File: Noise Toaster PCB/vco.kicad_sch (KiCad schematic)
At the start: 22 parts, among them Q3 2N3904, Q4 2N3904, U1 LM324

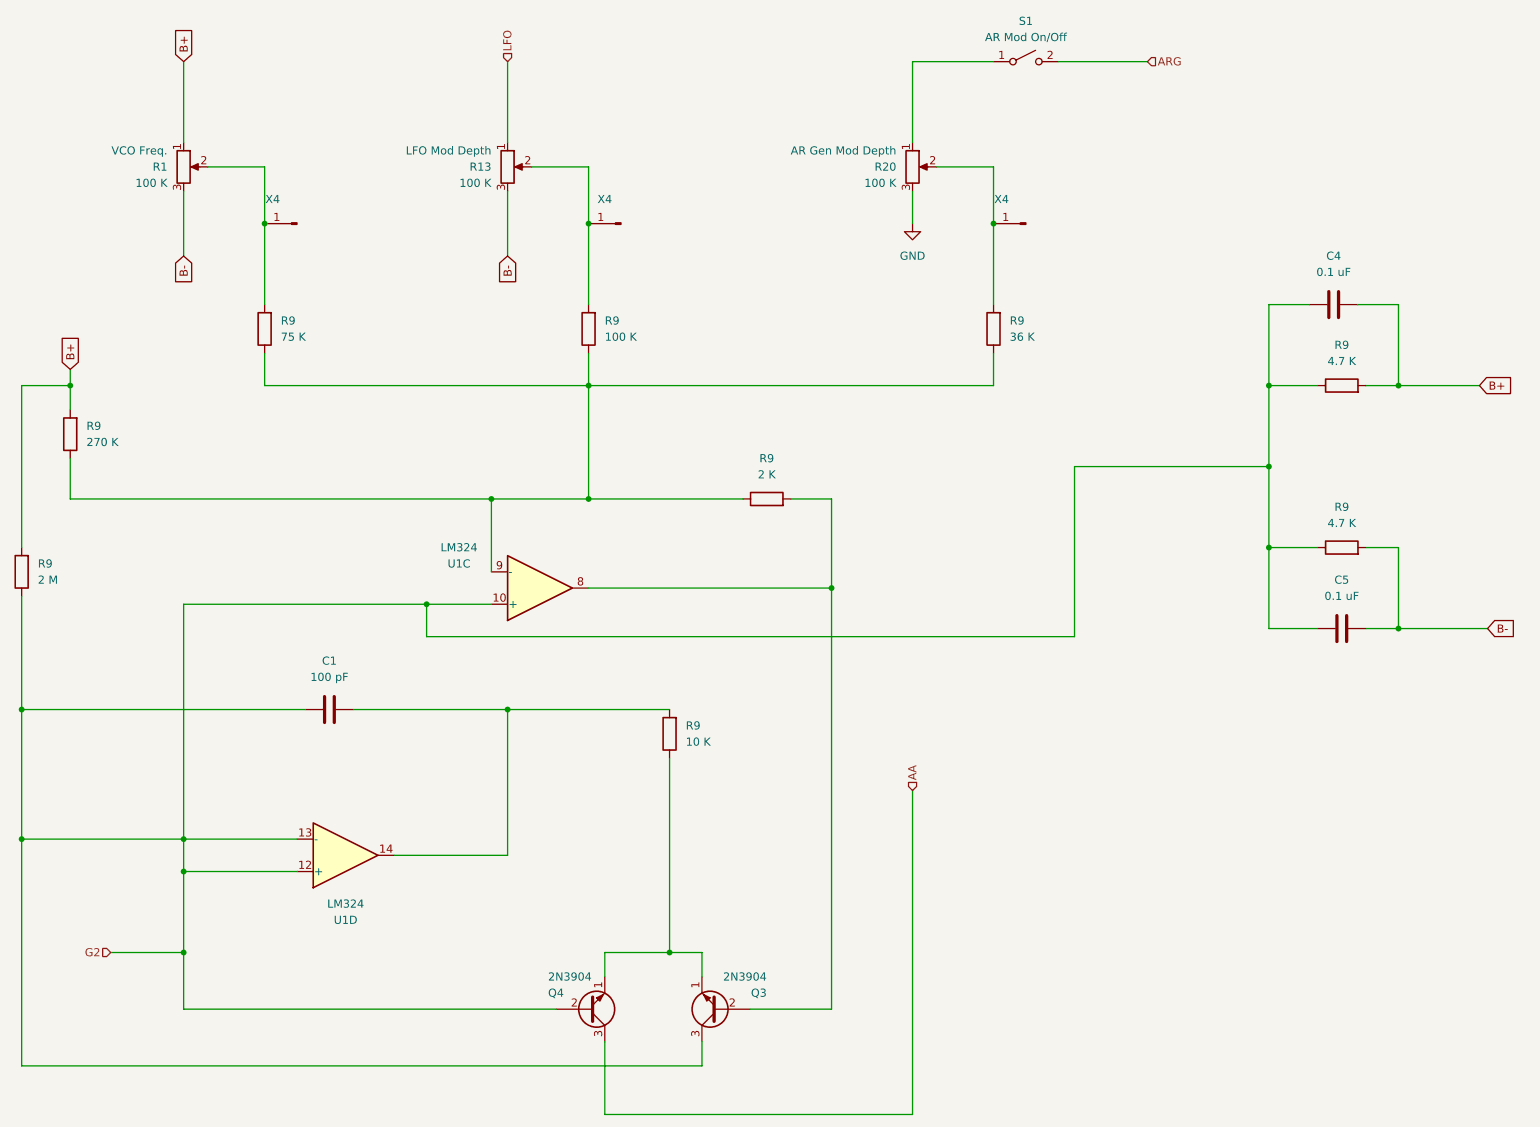
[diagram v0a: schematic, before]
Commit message: updated schematics
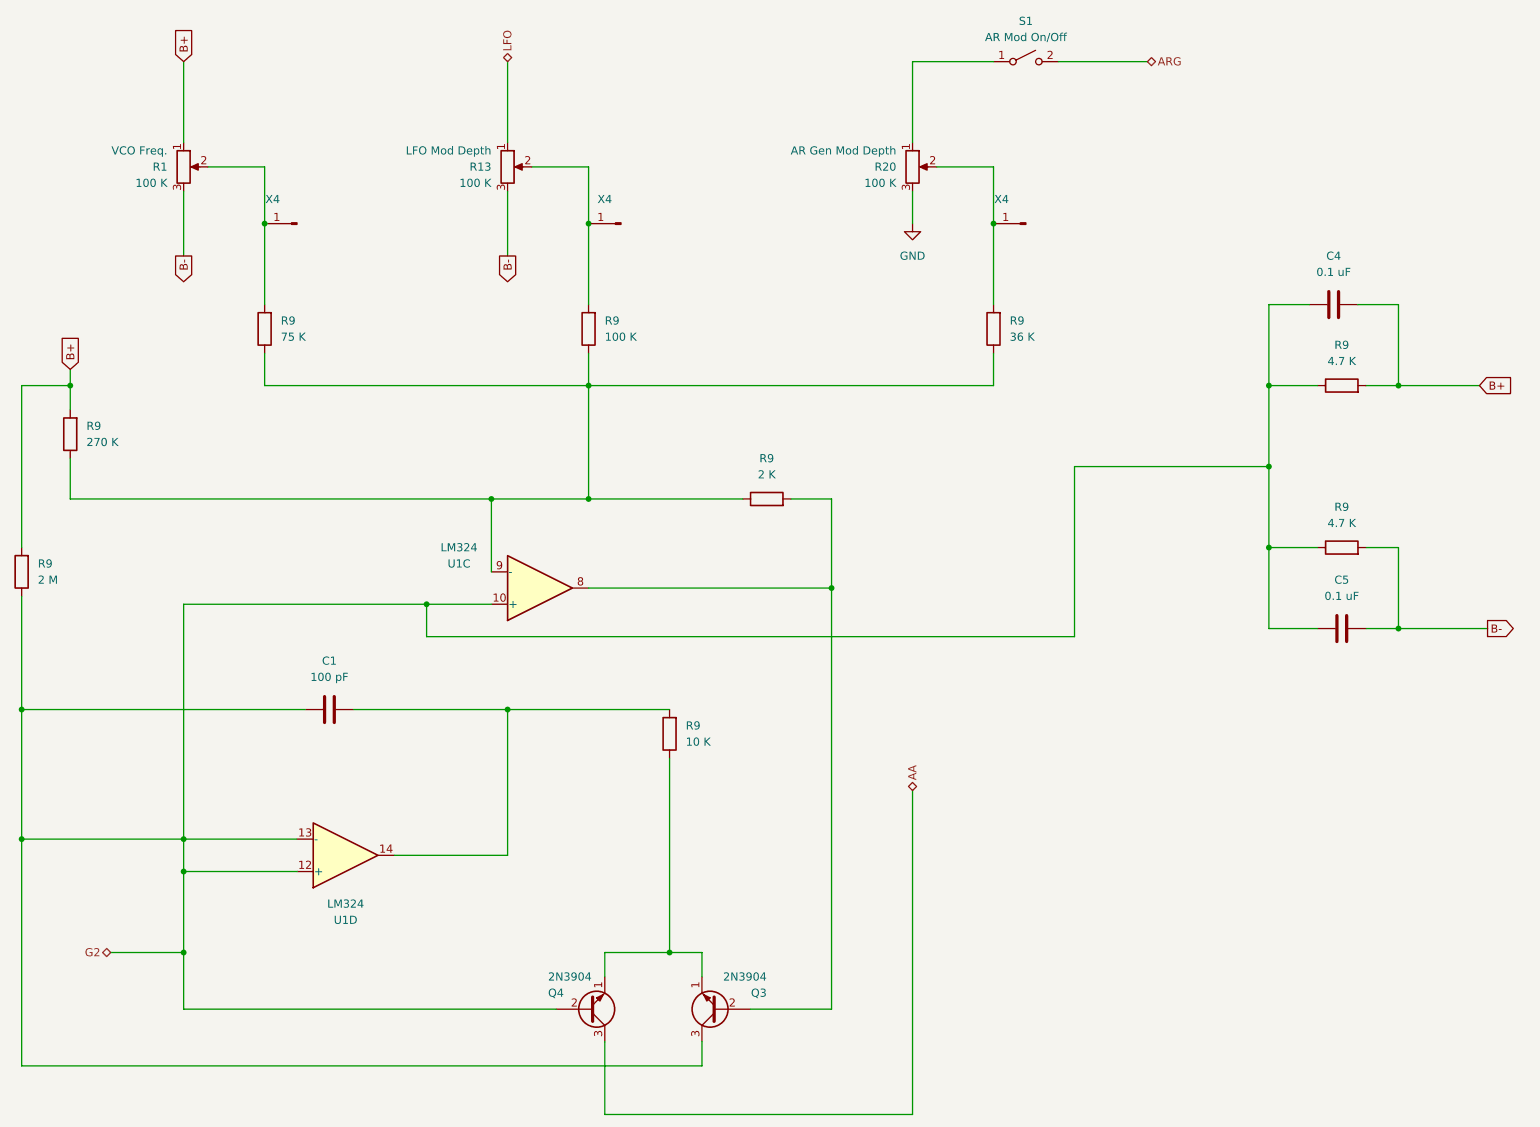
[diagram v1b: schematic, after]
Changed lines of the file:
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@@
     (stroke (width 0) (type default))
   )
-  (global_label "B-" (shape input) (at 255.27 114.3 0) (fields_autoplaced)
+  (global_label "B-" (shape output) (at 255.27 114.3 0) (fields_autoplaced)
     (effects (font (size 1.27 1.27)) (justify left))
     (property "Intersheetrefs" "${INTERSHEET_REFS}" (at 261.0976 114.3 0)
@@
     )
   )
-  (global_label "B-" (shape input) (at 50.8 55.88 270) (fields_autoplaced)
+  (global_label "B-" (shape output) (at 50.8 55.88 270) (fields_autoplaced)
     (effects (font (size 1.27 1.27)) (justify right))
     (property "Intersheetrefs" "${INTERSHEET_REFS}" (at 50.8 61.7076 90)
@@
     )
   )
-  (global_label "B-" (shape input) (at 101.6 55.88 270) (fields_autoplaced)
+  (global_label "B-" (shape output) (at 101.6 55.88 270) (fields_autoplaced)
     (effects (font (size 1.27 1.27)) (justify right))
     (property "Intersheetrefs" "${INTERSHEET_REFS}" (at 101.6 61.7076 90)
@@
     )
   )
-  (hierarchical_label "ARG" (shape input) (at 201.93 25.4 0) (fields_autoplaced)
-    (effects (font (size 1.27 1.27)) (justify left))
-  )
-  (hierarchical_label "G2" (shape input) (at 39.37 165.1 180) (fields_autoplaced)
+  (hierarchical_label "ARG" (shape bidirectional) (at 201.93 25.4 0) (fields_autoplaced)
+    (effects (font (size 1.27 1.27)) (justify left))
+  )
+  (hierarchical_label "G2" (shape bidirectional) (at 39.37 165.1 180) (fields_autoplaced)
     (effects (font (size 1.27 1.27)) (justify right))
   )
-  (hierarchical_label "LFO" (shape input) (at 101.6 25.4 90) (fields_autoplaced)
-    (effects (font (size 1.27 1.27)) (justify left))
-  )
-  (hierarchical_label "AA" (shape input) (at 165.1 139.7 90) (fields_autoplaced)
+  (hierarchical_label "LFO" (shape bidirectional) (at 101.6 25.4 90) (fields_autoplaced)
+    (effects (font (size 1.27 1.27)) (justify left))
+  )
+  (hierarchical_label "AA" (shape bidirectional) (at 165.1 139.7 90) (fields_autoplaced)
     (effects (font (size 1.27 1.27)) (justify left))
   )
@@
     (instances
       (project "Noise Toaster PCB"
-        (path "/7be3f398-d902-4566-9ee4-0bff072cd47e/9c6b1f0b-dddb-43c5-83ba-4fcd1cf28662"
-          (reference "#PWR01") (unit 1)
-        )
         (path "/7be3f398-d902-4566-9ee4-0bff072cd47e/d0369b76-3398-4137-86ba-22490a5aca99"
           (reference "#PWR03") (unit 1)

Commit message: refactored the schematic
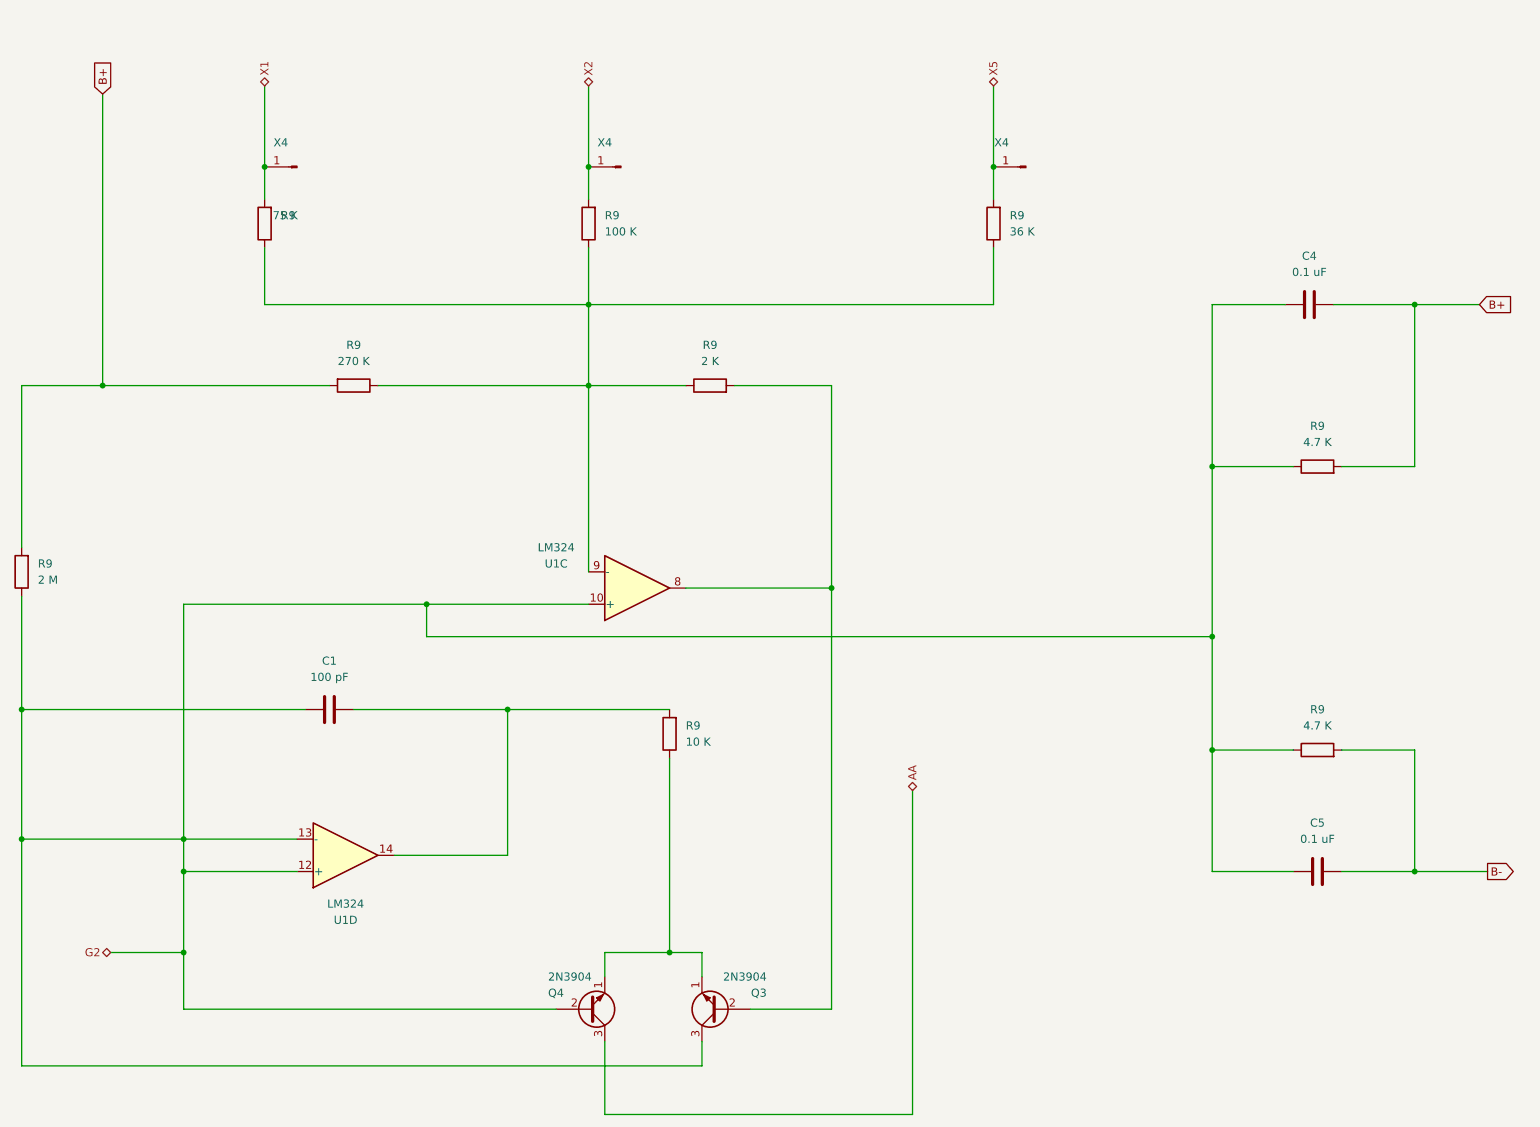
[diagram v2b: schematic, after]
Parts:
- removed R1, R13, R20: 100 K, symbol Device:R_Potentiometer
- removed S1: AR Mod On/Off, symbol Switch:SW_SPST
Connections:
- net X1: now reaches R9.2, X4.1 (Pin_1)
- net X5: now reaches R9.2, X4.1 (Pin_1)
- net X2: now reaches R9.2, X4.1 (Pin_1)
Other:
- moved on the sheet: C4, C5, R9, U1C, X4

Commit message: wireing and components have been checked
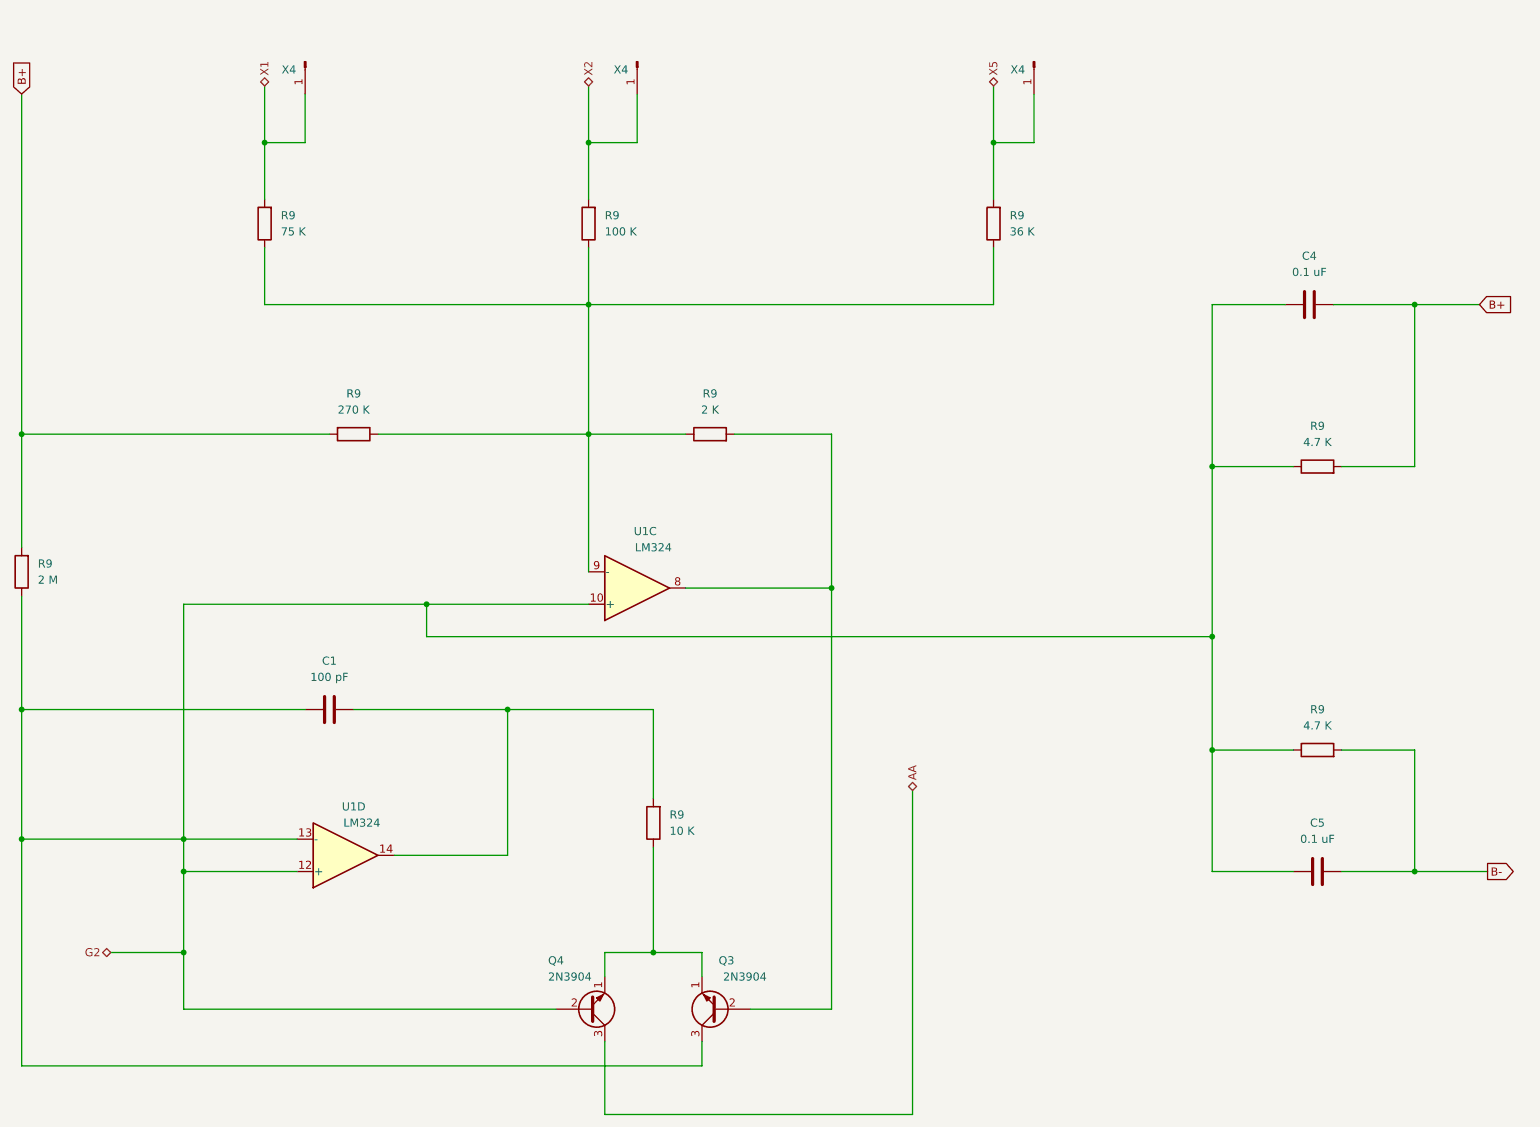
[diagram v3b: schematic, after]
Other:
- moved on the sheet: R9, X4

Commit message: applied footprints
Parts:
- C1, C4, C5: footprint (none) -> Capacitor_THT:C_Disc_D5.1mm_W3.2mm_P5.00mm
- R9: footprint (none) -> Resistor_THT:R_Axial_DIN0207_L6.3mm_D2.5mm_P10.16mm_Horizontal
- U1: footprint (none) -> Package_DIP:DIP-14_W7.62mm_Socket
- X4: footprint (none) -> Connector_PinHeader_1.00mm:PinHeader_1x01_P1.00mm_Vertical
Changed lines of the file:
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@@
       (effects (font (size 1.27 1.27)))
     )
-    (property "Footprint" "" (at 77.47 82.042 90)
+    (property "Footprint" "Resistor_THT:R_Axial_DIN0207_L6.3mm_D2.5mm_P10.16mm_Horizontal" (at 77.47 82.042 90)
       (effects (font (size 1.27 1.27)) hide)
     )
@@
       (effects (font (size 1.27 1.27)))
     )
-    (property "Footprint" "" (at 231.14 62.5348 0)
+    (property "Footprint" "Capacitor_THT:C_Disc_D5.1mm_W3.2mm_P5.00mm" (at 231.14 62.5348 0)
       (effects (font (size 1.27 1.27)) hide)
     )
@@
       (effects (font (size 1.27 1.27)))
     )
-    (property "Footprint" "" (at 228.6 90.678 90)
+    (property "Footprint" "Resistor_THT:R_Axial_DIN0207_L6.3mm_D2.5mm_P10.16mm_Horizontal" (at 228.6 90.678 90)
       (effects (font (size 1.27 1.27)) hide)
     )
@@
       (effects (font (size 1.27 1.27)))
     )
-    (property "Footprint" "" (at 74.93 152.4 0)
+    (property "Footprint" "Package_DIP:DIP-14_W7.62mm_Socket" (at 74.93 152.4 0)
       (effects (font (size 1.27 1.27)) hide)
     )
@@
       (effects (font (size 1.27 1.27)) (justify right))
     )
-    (property "Footprint" "" (at 27.178 105.41 90)
+    (property "Footprint" "Resistor_THT:R_Axial_DIN0207_L6.3mm_D2.5mm_P10.16mm_Horizontal" (at 27.178 105.41 90)
       (effects (font (size 1.27 1.27)) hide)
     )
@@
       (effects (font (size 1.27 1.27)))
     )
-    (property "Footprint" "" (at 77.47 126.0348 0)
+    (property "Footprint" "Capacitor_THT:C_Disc_D5.1mm_W3.2mm_P5.00mm" (at 77.47 126.0348 0)
       (effects (font (size 1.27 1.27)) hide)
     )
@@
       (effects (font (size 1.27 1.27)) (justify right))
     )
-    (property "Footprint" "" (at 65.278 50.8 90)
+    (property "Footprint" "Resistor_THT:R_Axial_DIN0207_L6.3mm_D2.5mm_P10.16mm_Horizontal" (at 65.278 50.8 90)
       (effects (font (size 1.27 1.27)) hide)
     )
@@
       (effects (font (size 1.27 1.27)))
     )
-    (property "Footprint" "" (at 232.41 151.4348 0)
+    (property "Footprint" "Capacitor_THT:C_Disc_D5.1mm_W3.2mm_P5.00mm" (at 232.41 151.4348 0)
       (effects (font (size 1.27 1.27)) hide)
     )
@@
       (effects (font (size 1.27 1.27)))
     )
-    (property "Footprint" "" (at 133.35 85.598 90)
+    (property "Footprint" "Resistor_THT:R_Axial_DIN0207_L6.3mm_D2.5mm_P10.16mm_Horizontal" (at 133.35 85.598 90)
       (effects (font (size 1.27 1.27)) hide)
     )
@@
       (effects (font (size 1.27 1.27)))
     )
-    (property "Footprint" "" (at 228.6 135.128 90)
+    (property "Footprint" "Resistor_THT:R_Axial_DIN0207_L6.3mm_D2.5mm_P10.16mm_Horizontal" (at 228.6 135.128 90)
       (effects (font (size 1.27 1.27)) hide)
     )
@@
       (effects (font (size 1.27 1.27)) (justify right))
     )
-    (property "Footprint" "" (at 126.238 144.78 90)
+    (property "Footprint" "Resistor_THT:R_Axial_DIN0207_L6.3mm_D2.5mm_P10.16mm_Horizontal" (at 126.238 144.78 90)
       (effects (font (size 1.27 1.27)) hide)
     )
@@
       (effects (font (size 1.27 1.27)) (justify right))
     )
-    (property "Footprint" "" (at 179.578 50.8 90)
+    (property "Footprint" "Resistor_THT:R_Axial_DIN0207_L6.3mm_D2.5mm_P10.16mm_Horizontal" (at 179.578 50.8 90)
       (effects (font (size 1.27 1.27)) hide)
     )
@@
       (effects (font (size 1.27 1.27)))
     )
-    (property "Footprint" "" (at 121.92 25.4 0)
+    (property "Footprint" "Connector_PinHeader_1.00mm:PinHeader_1x01_P1.00mm_Vertical" (at 121.92 25.4 0)
       (effects (font (size 1.27 1.27)) hide)
     )
@@
       (effects (font (size 1.27 1.27)))
     )
-    (property "Footprint" "" (at 120.65 110.49 0)
+    (property "Footprint" "Package_DIP:DIP-14_W7.62mm_Socket" (at 120.65 110.49 0)
       (effects (font (size 1.27 1.27)) hide)
     )
@@
       (effects (font (size 1.27 1.27)))
     )
-    (property "Footprint" "" (at 69.85 25.4 0)
+    (property "Footprint" "Connector_PinHeader_1.00mm:PinHeader_1x01_P1.00mm_Vertical" (at 69.85 25.4 0)
       (effects (font (size 1.27 1.27)) hide)
     )
@@
       (effects (font (size 1.27 1.27)))
     )
-    (property "Footprint" "" (at 184.15 25.4 0)
+    (property "Footprint" "Connector_PinHeader_1.00mm:PinHeader_1x01_P1.00mm_Vertical" (at 184.15 25.4 0)
       (effects (font (size 1.27 1.27)) hide)
     )
@@
       (effects (font (size 1.27 1.27)) (justify right))
     )
-    (property "Footprint" "" (at 116.078 50.8 90)
-      (effects (font (size 1.27 1.27)) hide)
-    )
+    (property "Footprint" "Resistor_THT:R_Axial_DIN0207_L6.3mm_D2.5mm_P10.16mm_Horizontal" (at 116.078 50.8 90)
+      (effects (font (size 1.27 1.27)) hide)
+    )
